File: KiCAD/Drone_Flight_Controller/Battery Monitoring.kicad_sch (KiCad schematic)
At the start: 7 parts, among them U205 AS358

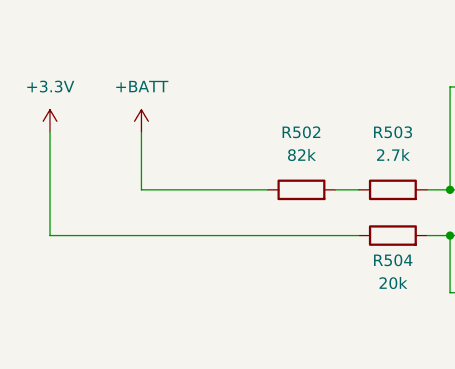
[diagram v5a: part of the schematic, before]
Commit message: Change "+3.3V" to "+3V3" for consistency
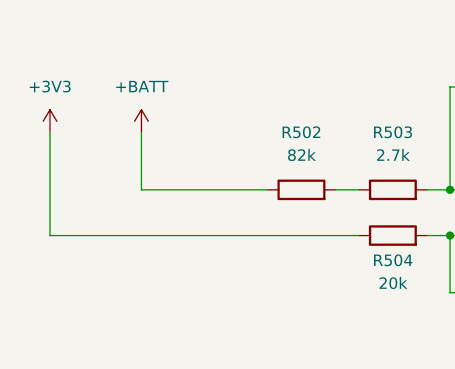
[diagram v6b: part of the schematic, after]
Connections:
- net +3.3V renamed +3V3
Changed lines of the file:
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@@
 	(title_block
 		(title "Battery Monitoring")
-		(date "2025-07-18")
-		(rev "V1")
+		(date "2025-09-19")
+		(rev "V2")
 		(company "HTL Steyr")
 		(comment 1 "Brandner")
@@
 		(dnp no)
 		(fields_autoplaced yes)
-		(property "Reference" "#PWR0502"
+		(property "Reference" "+3V3"
 			(at 40.64 36.83 0)
 			(effects
@@
 			)
 		)
-		(property "Value" "+3.3V"
+		(property "Value" "+3V3"
 			(at 40.64 27.94 0)
 			(effects
@@
 			(project ""
 				(path "/05daaa24-e506-4b9a-9564-8bf799413ca8/8aeacdae-c3f2-480a-a34d-37642627b117"
-					(reference "#PWR0502")
+					(reference "+3V3")
 					(unit 1)
 				)
